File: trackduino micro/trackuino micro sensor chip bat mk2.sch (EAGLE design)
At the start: 39 parts, among them IC2 74AHC1G125DBV, U1 ATMEGA328P, Y1 16MHZ

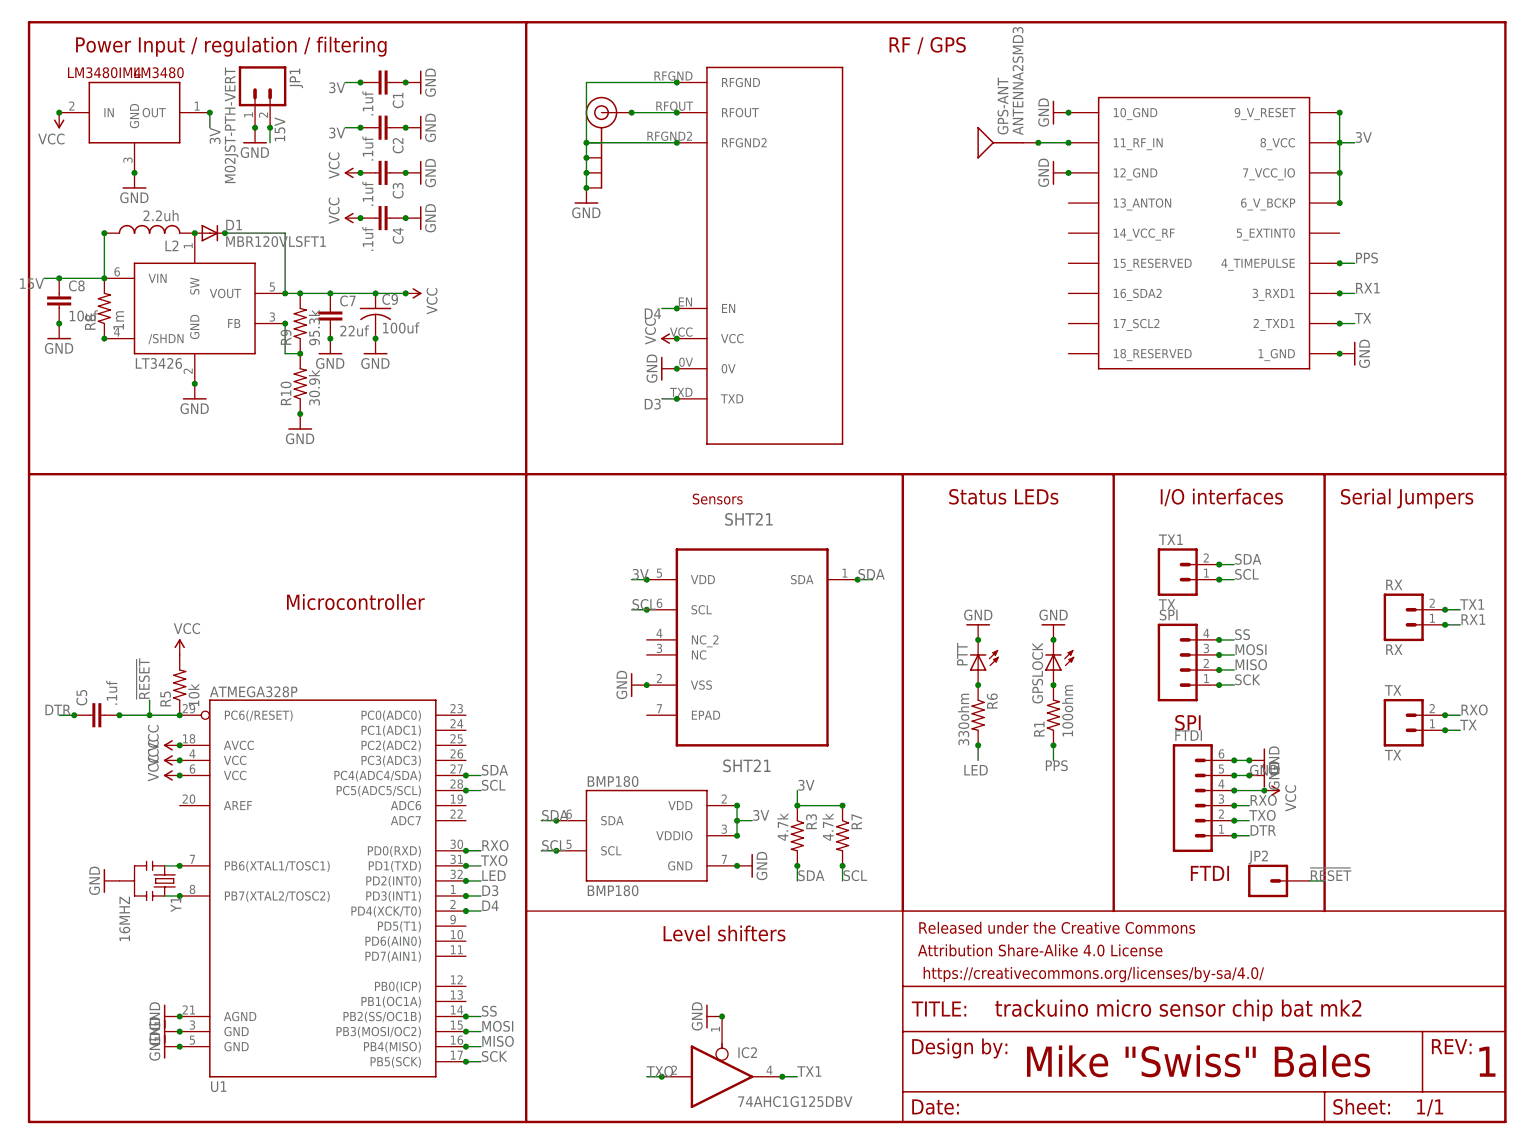
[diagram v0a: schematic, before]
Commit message: SilkScreen Clean Up and Battery
Cleaned up silk screen and created a board revision with a GPS backup
battery
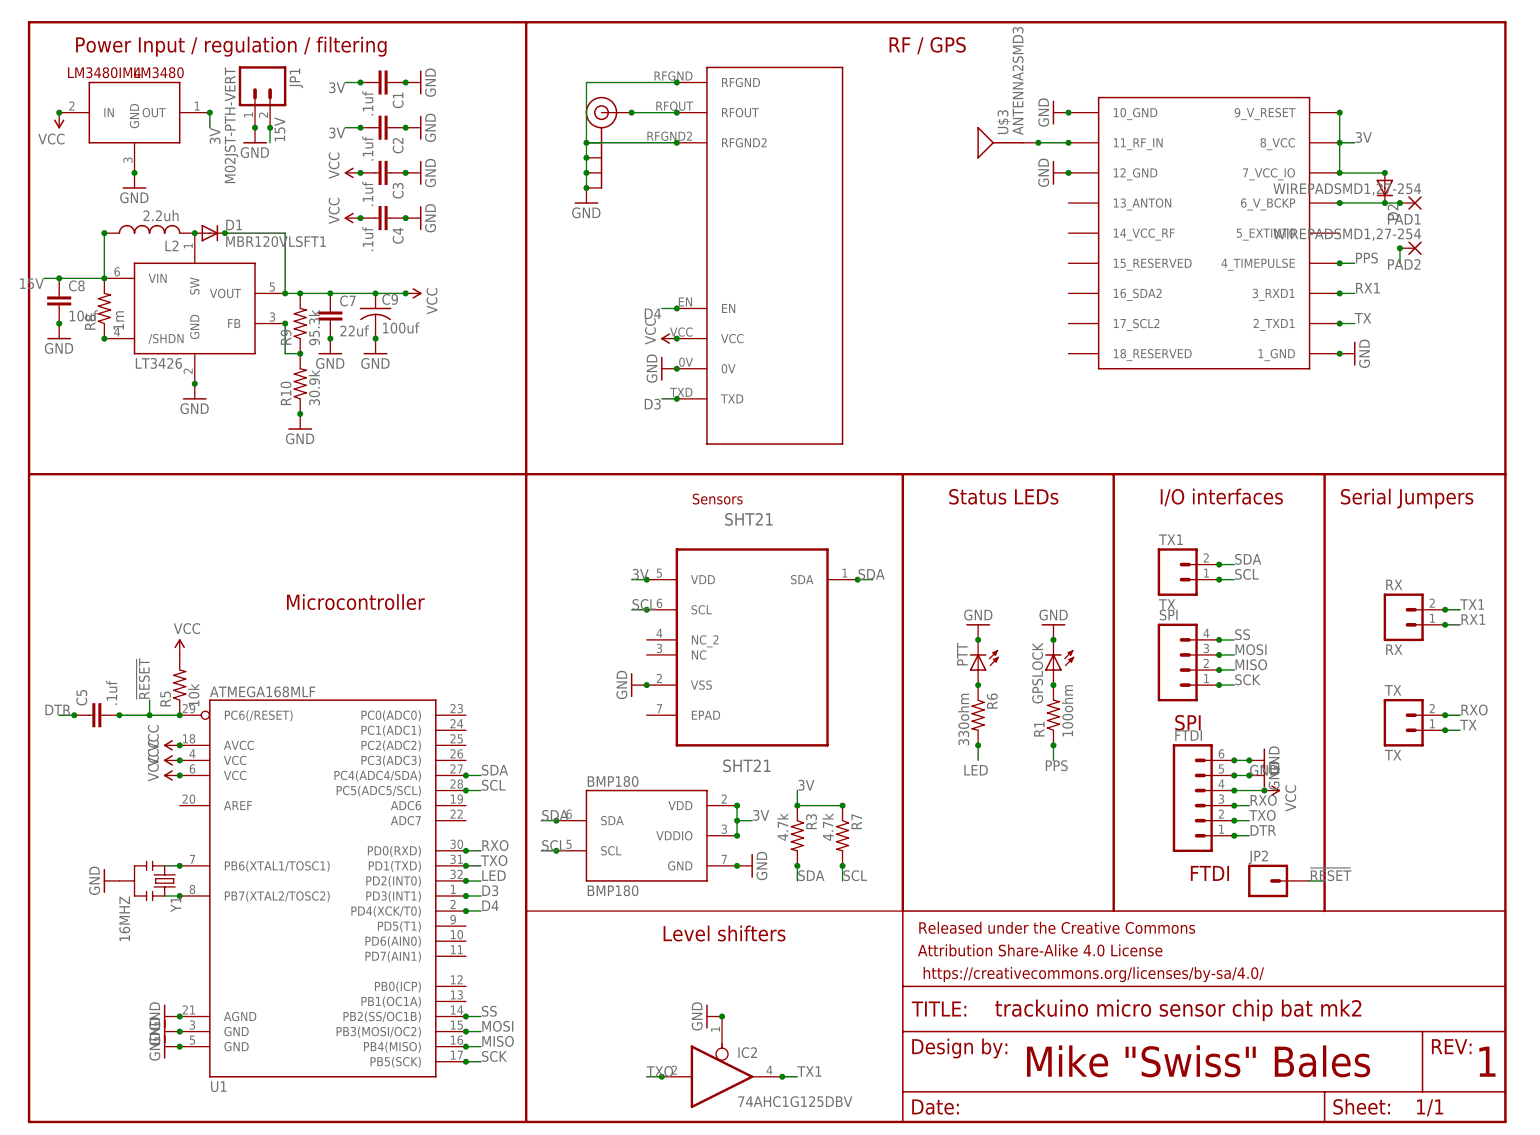
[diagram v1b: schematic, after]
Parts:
- added D2: (no value), diode:DIODE-MICROMELF-R
- added PAD1, PAD2: WIREPADSMD1,27-254, wirepad:WIREPADSMD1,27-254
- U1: value ATMEGA328P -> ATMEGA168MLF
- renumbered GPS-ANT to U$3
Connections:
- new net N$2: D2.C, PAD1.P, U$1.6_V_BCKP
- net 3V: now also D2.A; no longer U$1.6_V_BCKP
- net GND: now also PAD2.P
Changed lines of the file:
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@@
 <parts>
 <part name="IC2" library="74xx-little-us" deviceset="74*1G125" device="DBV" technology="AHC"/>
-<part name="U1" library="SparkFun-DigitalIC" deviceset="ATMEGA168" device="MLF" value="ATMEGA328P"/>
+<part name="U1" library="SparkFun-DigitalIC" deviceset="ATMEGA168" device="MLF" value="ATMEGA168MLF"/>
 <part name="U$2" library="Ava" deviceset="RADIOMETRIX-HX1" device=""/>
 <part name="LM3480" library="SparkFun-PowerIC" deviceset="LM3480IM4" device=""/>
@@
 <part name="GND31" library="SparkFun-Aesthetics" deviceset="GND" device=""/>
 <part name="SHT21" library="sht21" deviceset="SHT21" device=""/>
-<part name="GPS-ANT" library="SparkFun-RF" deviceset="ANTENNA2" device="SMD3"/>
+<part name="U$3" library="SparkFun-RF" deviceset="ANTENNA2" device="SMD3"/>
 <part name="TX1" library="SparkFun-Connectors" deviceset="M02" device="JST-PTH-VERT" value="TX"/>
 <part name="JP2" library="SparkFun-Connectors" deviceset="M01" device="PTH"/>
+<part name="PAD1" library="wirepad" deviceset="WIREPAD" device="SMD1,27-254"/>
+<part name="PAD2" library="wirepad" deviceset="WIREPAD" device="SMD1,27-254"/>
+<part name="D2" library="diode" deviceset="DIODE-" device="MICROMELF-R"/>
 </parts>
 <sheets>
@@
 <instance part="GND31" gate="1" x="58.42" y="129.54"/>
 <instance part="SHT21" gate="A" x="121.92" y="83.82"/>
-<instance part="GPS-ANT" gate="G$1" x="165.1" y="165.1" rot="R90"/>
+<instance part="U$3" gate="G$1" x="165.1" y="165.1" rot="R90"/>
 <instance part="TX1" gate="G$1" x="193.04" y="91.44"/>
 <instance part="JP2" gate="G$1" x="208.28" y="40.64"/>
+<instance part="PAD1" gate="G$1" x="233.68" y="154.94" rot="R180"/>
+<instance part="PAD2" gate="G$1" x="233.68" y="147.32" rot="R180"/>
+<instance part="D2" gate="G$1" x="228.6" y="157.48" rot="R270"/>
 </instances>
 <busses>
@@
 <junction x="104.14" y="73.66"/>
 </segment>
+<segment>
+<pinref part="PAD2" gate="G$1" pin="P"/>
+<wire x1="231.14" y1="147.32" x2="231.14" y2="144.78" width="0.1524" layer="91"/>
+<junction x="231.14" y="147.32"/>
+</segment>
 </net>
 <net name="D3" class="0">
@@
 <pinref part="U$1" gate="G$1" pin="7_VCC_IO"/>
 <wire x1="220.98" y1="170.18" x2="220.98" y2="165.1" width="0.1524" layer="91"/>
-<junction x="220.98" y="160.02"/>
 <junction x="220.98" y="165.1"/>
 <wire x1="220.98" y1="165.1" x2="220.98" y2="160.02" width="0.1524" layer="91"/>
 <junction x="220.98" y="170.18"/>
-<pinref part="U$1" gate="G$1" pin="6_V_BCKP"/>
-<wire x1="220.98" y1="160.02" x2="220.98" y2="154.94" width="0.1524" layer="91"/>
-<junction x="220.98" y="154.94"/>
+<junction x="220.98" y="160.02"/>
+<pinref part="D2" gate="G$1" pin="A"/>
+<wire x1="228.6" y1="160.02" x2="220.98" y2="160.02" width="0.1524" layer="91"/>
+<junction x="228.6" y="160.02"/>
 </segment>
 <segment>
@@
 <segment>
 <pinref part="U$1" gate="G$1" pin="11_RF_IN"/>
-<pinref part="GPS-ANT" gate="G$1" pin="SIGNAL"/>
+<pinref part="U$3" gate="G$1" pin="SIGNAL"/>
 <wire x1="170.18" y1="165.1" x2="175.26" y2="165.1" width="0.1524" layer="91"/>
 <junction x="170.18" y="165.1"/>
@@
 </segment>
 </net>
+<net name="N$2" class="0">
+<segment>
+<pinref part="U$1" gate="G$1" pin="6_V_BCKP"/>
+<wire x1="220.98" y1="154.94" x2="228.6" y2="154.94" width="0.1524" layer="91"/>
+<pinref part="PAD1" gate="G$1" pin="P"/>
+<junction x="231.14" y="154.94"/>
+<junction x="220.98" y="154.94"/>
+<pinref part="D2" gate="G$1" pin="C"/>
+<wire x1="228.6" y1="154.94" x2="231.14" y2="154.94" width="0.1524" layer="91"/>
+<junction x="228.6" y="154.94"/>
+</segment>
+</net>
